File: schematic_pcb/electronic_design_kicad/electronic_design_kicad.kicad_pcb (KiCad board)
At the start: 2 copper layers, 34.3 x 18.2 mm, 20 parts, among them IC1 ATTINY85-S, P1 USB_A, P2 CONN_6

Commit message: added 3d design files and finished schematic and PCB
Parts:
- moved R8 6.91 mm to (161.5, 187.1), turned to 270 degrees
- moved R7 6.14 mm to (165.0, 186.2), turned to 180 degrees
- moved P2 4.52 mm to (163.0, 182.4)
- moved R4 4.50 mm to (162.2, 177.7)
- moved C1 4.10 mm to (157.6, 177.6), turned to 180 degrees
- moved D2 4.03 mm to (170.2, 185.1), turned to 180 degrees
- moved D3 3.81 mm to (170.2, 179.6), turned to 180 degrees
- moved R10 3.64 mm to (166.2, 183.5)
- moved R11 3.64 mm to (166.2, 181.2)
- moved area0x33 2.73 mm to (150.7, 182.4)
- moved R6 0.50 mm to (166.7, 177.6), turned to 0 degrees
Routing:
- net /RIGHT: track 19.2 -> 4.48 mm
- net DGND: track 40.9 -> 48.4 mm, vias 3 -> 1
- net Net-(D3-Pad2): track 10.5 -> 3.68 mm
- net /LEFT: track 0.00 -> 6.38 mm, vias 0 -> 1
- net /ADC: track 10.3 -> 15.2 mm
- net /DOWN: track 9.72 -> 14.0 mm, vias 1 -> 2
- net +5V: track 32.7 -> 29.7 mm
- net /G: track 5.65 -> 3.02 mm
- net /R: track 5.45 -> 3.43 mm

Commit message: added gerber files for manufacture
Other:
- board size 34.3 x 18.2 mm -> 34.3 x 13.6 mm
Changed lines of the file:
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@@
     (links 36)
     (no_connects 0)
-    (area 134.413658 173.203669 174.71366 191.510331)
+    (area 134.413658 173.273843 174.71366 192.700504)
     (thickness 1.6)
-    (drawings 2754)
+    (drawings 2758)
     (tracks 126)
     (zones 0)
@@
     (zone_45_only yes)
     (trace_min 0.1524)
-    (segment_width 0.2)
-    (edge_width 0.1)
+    (segment_width 0.01)
+    (edge_width 0.01)
     (via_size 0.9)
     (via_drill 0.5)
@@
     (solder_mask_min_width 0.2)
     (aux_axis_origin 132.969 189.357)
-    (visible_elements 7FFFFFFF)
+    (visible_elements 7FFEFDFF)
     (pcbplotparams
-      (layerselection 0x01000_00000000)
+      (layerselection 0x010f0_80000001)
       (usegerberextensions false)
       (excludeedgelayer true)
@@
       (padsonsilk false)
       (subtractmaskfromsilk false)
-      (outputformat 4)
+      (outputformat 1)
       (mirror false)
       (drillshape 0)
@@
     (descr "USB A connector")
     (tags "USB USB_A")
-    (fp_text reference P1 (at 0 2 90) (layer B.SilkS)
+    (fp_text reference P1 (at 0.107 7.281 90) (layer B.SilkS)
       (effects (font (size 0.65 0.65) (thickness 0.13)) (justify mirror))
     )
@@
     (fp_line (start -6.8 6.5) (end -6.8 0) (layer B.SilkS) (width 0.15))
     (fp_line (start -6.8 0) (end 6.8 0) (layer B.SilkS) (width 0.15))
-    (pad "" thru_hole circle (at -5.4 7.5 90) (size 1.4 1.4) (drill 1.4) (layers *.Cu *.Mask B.SilkS))
-    (pad "" thru_hole circle (at 5.4 7.5 90) (size 1.4 1.4) (drill 1.4) (layers *.Cu *.Mask B.SilkS))
-    (pad "" thru_hole circle (at 2.3 2.9 90) (size 1.2 1.2) (drill 1.2) (layers *.Cu *.Mask B.SilkS))
-    (pad "" thru_hole circle (at -2.3 2.9 180) (size 1.2 1.2) (drill 1.2) (layers *.Cu *.Mask B.SilkS))
+    (pad "" np_thru_hole circle (at -5.4 7.5 90) (size 1.4 1.4) (drill 1.4) (layers *.Cu *.Mask B.SilkS))
+    (pad "" np_thru_hole circle (at 5.4 7.5 90) (size 1.4 1.4) (drill 1.4) (layers *.Cu *.Mask B.SilkS))
+    (pad "" np_thru_hole circle (at 2.3 2.9 90) (size 1.2 1.2) (drill 1.2) (layers *.Cu *.Mask B.SilkS))
+    (pad "" np_thru_hole circle (at -2.3 2.9 180) (size 1.2 1.2) (drill 1.2) (layers *.Cu *.Mask B.SilkS))
     (pad 1 thru_hole circle (at 3.5 5 180) (size 1.5 1.5) (drill 1.00076) (layers *.Cu *.Mask B.SilkS)
       (net 1 +5V))
@@
     (at 165 186.25 180)
     (attr smd)
-    (fp_text reference R7 (at 1 -1.75 360) (layer F.SilkS)
+    (fp_text reference R7 (at -2.35 -0.6 360) (layer F.SilkS)
       (effects (font (size 0.65 0.65) (thickness 0.13)))
     )
@@
     (at 166.25 183.5)
     (attr smd)
-    (fp_text reference R10 (at 0 -2 90) (layer F.SilkS)
+    (fp_text reference R10 (at 2.65 -0.6 180) (layer F.SilkS)
       (effects (font (size 0.65 0.65) (thickness 0.13)))
     )
@@
     (at 166.25 181.25)
     (attr smd)
-    (fp_text reference R11 (at -0.85 -1.55) (layer F.SilkS)
+    (fp_text reference R11 (at 2.65 0.55) (layer F.SilkS)
       (effects (font (size 0.65 0.65) (thickness 0.13)))
     )
@@
     )
   )
+  (gr_line (start 140 188.25) (end 141.7 188.25) (angle 90) (layer Dwgs.User) (width 0.6))
+  (gr_line (start 140 176.5) (end 141.7 176.5) (angle 90) (layer Dwgs.User) (width 0.6))
+  (gr_circle (center 151.86 189.96) (end 152.56 191.16) (layer Dwgs.User) (width 0.01))
+  (gr_circle (center 151.86 174.76) (end 152.74 175.84) (layer Dwgs.User) (width 0.01))
+  (gr_line (start 137.97 175.56) (end 150.73 175.56) (angle 90) (layer Edge.Cuts) (width 0.01))
+  (gr_line (start 152.99 175.56) (end 168.97 175.56) (angle 90) (layer Edge.Cuts) (width 0.01))
+  (gr_arc (start 151.86 174.76) (end 152.99 175.56) (angle 109.4) (layer Edge.Cuts) (width 0.01))
+  (gr_line (start 168.97 189.16) (end 152.99 189.16) (angle 90) (layer Edge.Cuts) (width 0.01))
+  (gr_line (start 137.97 189.16) (end 150.73 189.16) (angle 90) (layer Edge.Cuts) (width 0.01))
+  (gr_arc (start 151.86 189.96) (end 150.73 189.16) (angle 109.4) (layer Edge.Cuts) (width 0.01))
   (dimension 34.250036 (width 0.025) (layer Dwgs.User)
     (gr_text "34.250 mm" (at 155.070036 192.575503 359.9163566) (layer Dwgs.User)
@@
     (arrow2b (pts (xy 137.945182 192.450503) (xy 139.072541 191.865727)))
   )
-  (dimension 13.6 (width 0.025) (layer Dwgs.User)
-    (gr_text "13.600 mm" (at 176.449999 182.35 270) (layer Dwgs.User)
-      (effects (font (size 0.1 0.1) (thickness 0.025)))
-    )
-    (feature1 (pts (xy 168.95 189.15) (xy 176.549999 189.15)))
-    (feature2 (pts (xy 168.95 175.55) (xy 176.549999 175.55)))
-    (crossbar (pts (xy 176.349999 175.55) (xy 176.349999 189.15)))
-    (arrow1a (pts (xy 176.349999 189.15) (xy 175.763578 188.023496)))
-    (arrow1b (pts (xy 176.349999 189.15) (xy 176.93642 188.023496)))
-    (arrow2a (pts (xy 176.349999 175.55) (xy 175.763578 176.676504)))
-    (arrow2b (pts (xy 176.349999 175.55) (xy 176.93642 176.676504)))
-  )
-  (gr_circle (center 151.869 174.757) (end 151.969 173.257) (layer Edge.Cuts) (width 0.1))
-  (gr_circle (center 151.869 189.957) (end 151.969 188.457) (layer Edge.Cuts) (width 0.1))
-  (gr_line (start 168.969 175.557) (end 137.969 175.557) (angle 90) (layer Edge.Cuts) (width 0.1))
-  (gr_line (start 168.969 189.157) (end 137.969 189.157) (angle 90) (layer Edge.Cuts) (width 0.1))
-  (gr_line (start 172.269 185.857) (end 172.269 178.857) (angle 90) (layer Edge.Cuts) (width 0.1))
-  (gr_line (start 168.969 189.157) (end 172.269 185.857) (angle 90) (layer Edge.Cuts) (width 0.1))
-  (gr_line (start 168.969 175.557) (end 172.269 178.857) (angle 90) (layer Edge.Cuts) (width 0.1))
-  (gr_line (start 137.969 175.557) (end 137.969 189.157) (angle 90) (layer Edge.Cuts) (width 0.1))
+  (gr_line (start 172.269 185.857) (end 172.269 178.857) (angle 90) (layer Edge.Cuts) (width 0.01))
+  (gr_line (start 168.969 189.157) (end 172.269 185.857) (angle 90) (layer Edge.Cuts) (width 0.01))
+  (gr_line (start 168.969 175.557) (end 172.269 178.857) (angle 90) (layer Edge.Cuts) (width 0.01))
+  (gr_line (start 137.969 175.557) (end 137.969 189.157) (angle 90) (layer Edge.Cuts) (width 0.01))
   (gr_line (start 157.463659 175.307508) (end 157.463659 189.414188) (layer Dwgs.User) (width 0.1))
   (gr_line (start 145.963659 175.307508) (end 145.963659 189.414188) (layer Dwgs.User) (width 0.1))
@@
   (gr_line (start 172.163659 176.650848) (end 172.163659 176.470848) (layer Dwgs.User) (width 0.1))
   (gr_line (start 172.073659 176.560848) (end 172.253659 176.560848) (layer Dwgs.User) (width 0.1))
-  (gr_line (start 172.732898 175.825411) (end 172.843073 175.683069) (layer Dwgs.User) (width 0.1))
   (gr_line (start 151.801159 189.960848) (end 151.683659 189.960848) (layer Dwgs.User) (width 0.1))
   (gr_line (start 151.801159 174.760848) (end 151.683659 174.760848) (layer Dwgs.User) (width 0.1))

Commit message: memtype hardware revision 2.1
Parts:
- D2, D3: footprint LEDs:LED_0603 -> projectLib:LED_0603_PIPE
- P1: footprint USB_A_MALE -> projectLib:USB_A_MALE
- P2: footprint projectLib:SKRHAAE010 -> SKRHAAE010
- R10, R11: value 68R -> 220R
- R9: value 1M -> 560k
- moved P2 2.67 mm to (160.3, 182.4)
- moved D2 2.08 mm to (168.2, 184.6)
- moved R6 2.06 mm to (168.4, 178.8), turned to 270 degrees
- moved D3 2.02 mm to (168.2, 179.6)
- moved R10 1.70 mm to (167.8, 184.2), turned to 270 degrees
- moved R11 1.63 mm to (165.2, 180.0), turned to 90 degrees
- moved C1 1.37 mm to (156.2, 177.6), turned to 0 degrees
- moved R7 0.84 mm to (164.2, 186.0), turned to 90 degrees
- moved R8 0.52 mm to (161.6, 186.6)
- moved R5 0.48 mm to (159.2, 186.6)
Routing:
- net /LEFT: track 6.38 -> 17.6 mm
- net /DOWN: track 14.0 -> 17.8 mm, vias 2 -> 1
- net /ADC: track 15.2 -> 12.1 mm
- net +5V: track 29.7 -> 32.5 mm
- net /G: track 3.02 -> 5.65 mm
- net /RIGHT: track 4.48 -> 7.04 mm
- net DGND: track 48.4 -> 47.3 mm
- net Net-(D3-Pad2): track 3.68 -> 2.77 mm
- net Net-(D2-Pad2): track 3.66 -> 3.02 mm
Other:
- board size 34.3 x 13.6 mm -> 34.2 x 13.6 mm

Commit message: update joystick direction in schematic and code
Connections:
- P2 pad 3: /LEFT -> /UP
- P2 pad 6: /RIGHT -> /LEFT
- R4 pad 2: /LEFT -> /UP
- R6 pad 1: /LEFT -> /UP
- R7 pad 2: /RIGHT -> /LEFT
- R8 pad 1: /RIGHT -> /LEFT
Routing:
- net /UP: track 0.00 -> 17.6 mm, vias 0 -> 1
- net /LEFT: track 17.6 -> 7.04 mm
- net /RIGHT: track 7.04 -> 0.00 mm, vias 1 -> 0

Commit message: hardware revision 3.0
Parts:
- removed D2: LED GREEN, projectLib:LED_0603_PIPE
- removed R10: 220R, projectLib:SMD-0805
- added R12: 1k, projectLib:SMD-0805, F.Cu at (156.8, 186.8)
- P2: footprint SKRHAAE010 -> projectLib:SKRHAAE010
- moved D3 11.7 mm to (156.9, 182.4)
- moved P2 10.1 mm to (150.2, 182.2)
- moved area0x33 9.73 mm to (159.5, 178.2)
- moved R6 6.40 mm to (162.0, 178.8)
- moved R5 4.70 mm to (154.5, 186.8)
- moved R9 4.61 mm to (152.2, 186.8)
- moved C2 4.57 mm to (150.0, 186.8)
- moved R11 4.12 mm to (162.0, 182.6), turned to 270 degrees
- moved IC1 3.87 mm to (154.6, 181.4)
- moved R4 3.78 mm to (158.4, 177.4)
- moved D1 3.26 mm to (146.8, 186.2)
- moved R1 3.24 mm to (146.8, 178.0)
- moved R2 3.18 mm to (146.8, 180.4)
- moved R3 3.17 mm to (146.8, 182.6)
- moved R7 2.19 mm to (162.2, 187.0), turned to 270 degrees
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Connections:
- IC1 pad 5: /G -> (no net)
- P2 pad 2: (no net) -> /CENTER
- R8 pad 2: DGND -> /CENTER
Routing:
- net /CENTER: track 0.00 -> 23.2 mm, vias 0 -> 1
- net DGND: track 47.3 -> 38.2 mm
- net /G: track 5.65 -> 0.00 mm
- net /LEFT: track 7.04 -> 12.4 mm
- net Net-(C2-Pad1): track 30.9 -> 25.6 mm
- net +5V: track 32.5 -> 28.7 mm, vias 1 -> 0
- net Net-(D3-Pad2): track 2.77 -> 6.38 mm
- net Net-(D2-Pad2): track 3.02 -> 0.00 mm, vias 1 -> 0
- net D+: track 8.25 -> 5.34 mm
- net /DOWN: track 17.8 -> 20.7 mm
- net D-: track 13.4 -> 11.2 mm
- net /ADC: track 12.1 -> 13.6 mm
- net /UP: track 17.6 -> 18.5 mm
- net Net-(IC1-Pad3): track 3.99 -> 3.27 mm
- net Net-(IC1-Pad2): track 3.89 -> 3.21 mm
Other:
- board size 34.2 x 13.6 mm -> 25.5 x 14.5 mm

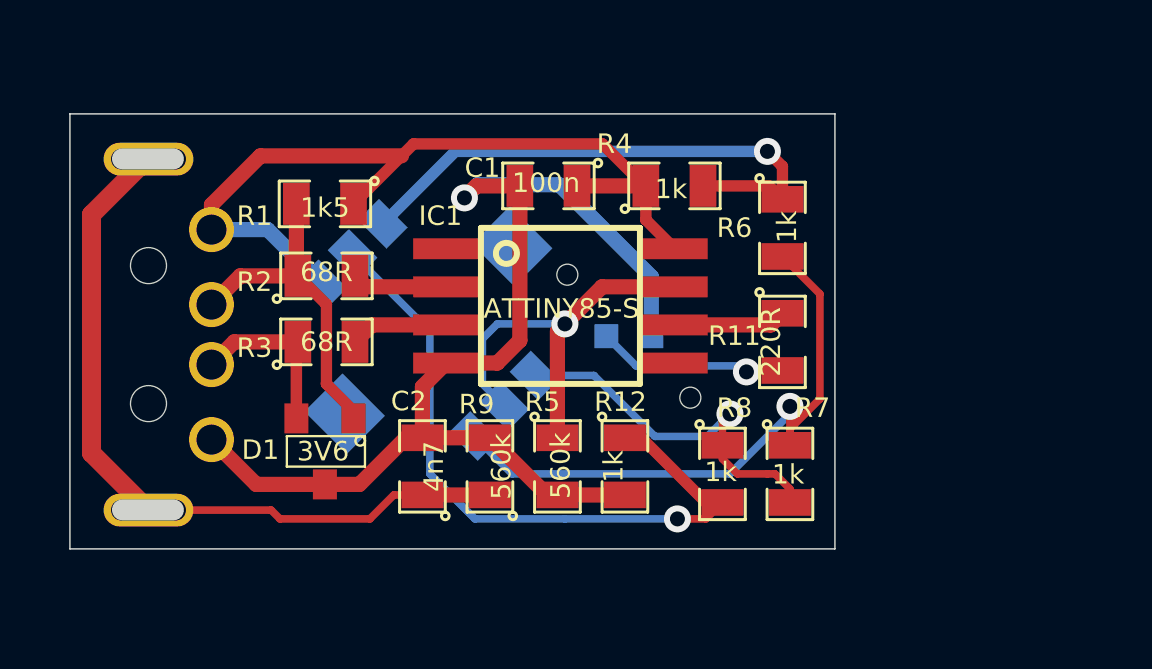
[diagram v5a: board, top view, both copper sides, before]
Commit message: Added consistency between Schematic and Code
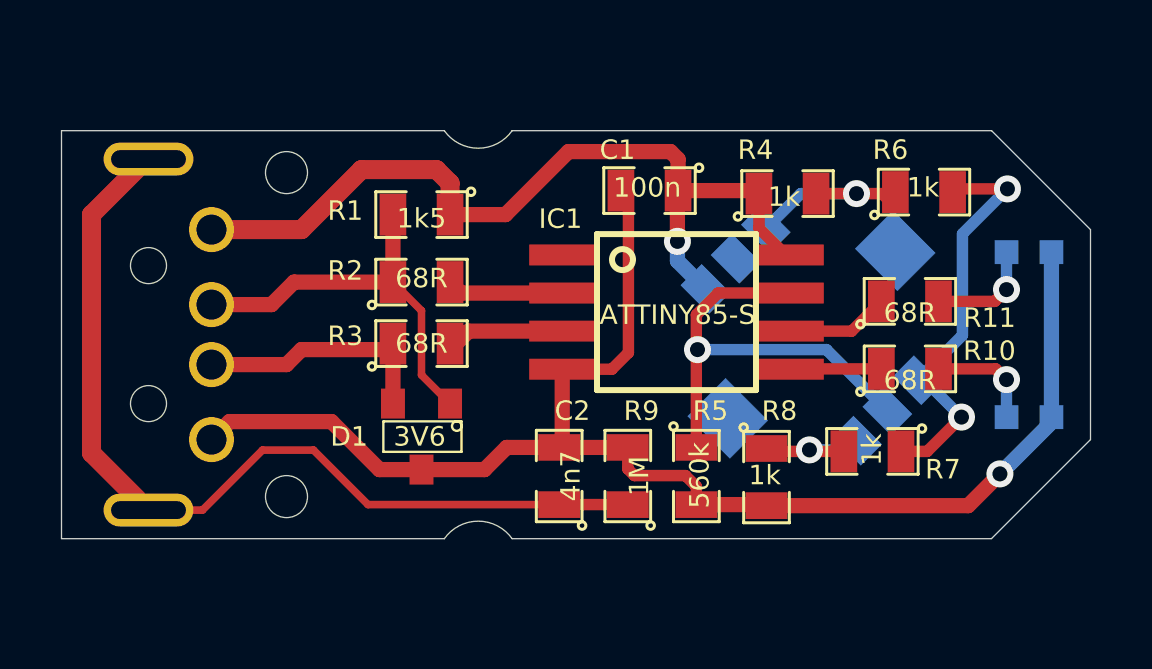
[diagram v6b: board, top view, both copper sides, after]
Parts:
- removed R12: 1k, projectLib:SMD-0805
- added D2: LED GREEN, LEDs:LED_0603, B.Cu at (170.2, 185.1)
- added R10: 68R, projectLib:SMD-0805, F.Cu at (166.2, 183.5)
- D3: footprint projectLib:LED_0603_PIPE -> LEDs:LED_0603
- P1: footprint projectLib:USB_A_MALE -> USB_A_MALE
- R11: value 220R -> 68R
- R9: value 560k -> 1M
- moved D3 13.6 mm to (170.2, 179.6)
- moved P2 12.8 mm to (163.0, 182.4)
- moved area0x33 9.73 mm to (150.7, 182.4)
- moved R6 4.87 mm to (166.7, 177.6), turned to 0 degrees
- moved R5 4.64 mm to (159.1, 187.1)
- moved R9 4.61 mm to (156.8, 187.1)
- moved C2 4.57 mm to (154.6, 187.1)
- moved R11 4.46 mm to (166.2, 181.2), turned to 0 degrees
- moved IC1 3.87 mm to (158.5, 181.6)
- moved R4 3.78 mm to (162.2, 177.7)
- moved C1 3.37 mm to (157.6, 177.6)
- moved D1 3.26 mm to (150.0, 185.8)
- moved R1 3.24 mm to (150.0, 178.4)
- moved R2 3.18 mm to (150.0, 180.6)
- moved R3 3.17 mm to (150.0, 182.7)
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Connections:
- IC1 pad 5: (no net) -> /G
- P2 pad 2: /CENTER -> (no net)
- P2 pad 3: /UP -> /LEFT
- P2 pad 6: /LEFT -> /RIGHT
- R4 pad 2: /UP -> /LEFT
- R6 pad 1: /UP -> /LEFT
- R7 pad 2: /LEFT -> /RIGHT
- R8 pad 1: /LEFT -> /RIGHT
- R8 pad 2: /CENTER -> DGND
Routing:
- net /CENTER: track 23.2 -> 0.00 mm, vias 1 -> 0
- net /UP: track 18.5 -> 0.00 mm, vias 1 -> 0
- net DGND: track 38.2 -> 48.4 mm
- net /DOWN: track 20.7 -> 14.0 mm, vias 1 -> 2
- net /LEFT: track 12.4 -> 6.38 mm
- net Net-(C2-Pad1): track 25.6 -> 30.9 mm
- net /RIGHT: track 0.00 -> 4.48 mm, vias 0 -> 1
- net Net-(D2-Pad2): track 0.00 -> 3.66 mm, vias 0 -> 1
- net /G: track 0.00 -> 3.02 mm
- net D+: track 5.34 -> 8.25 mm
- net Net-(D3-Pad2): track 6.38 -> 3.68 mm
- net D-: track 11.2 -> 13.4 mm
- net /ADC: track 13.6 -> 15.2 mm
- net +5V: track 28.7 -> 29.7 mm, vias 0 -> 1
- net Net-(IC1-Pad3): track 3.27 -> 3.99 mm
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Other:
- board size 25.5 x 14.5 mm -> 34.3 x 13.6 mm
